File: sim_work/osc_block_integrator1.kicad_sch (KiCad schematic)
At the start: 6 parts, among them U2 LM4562

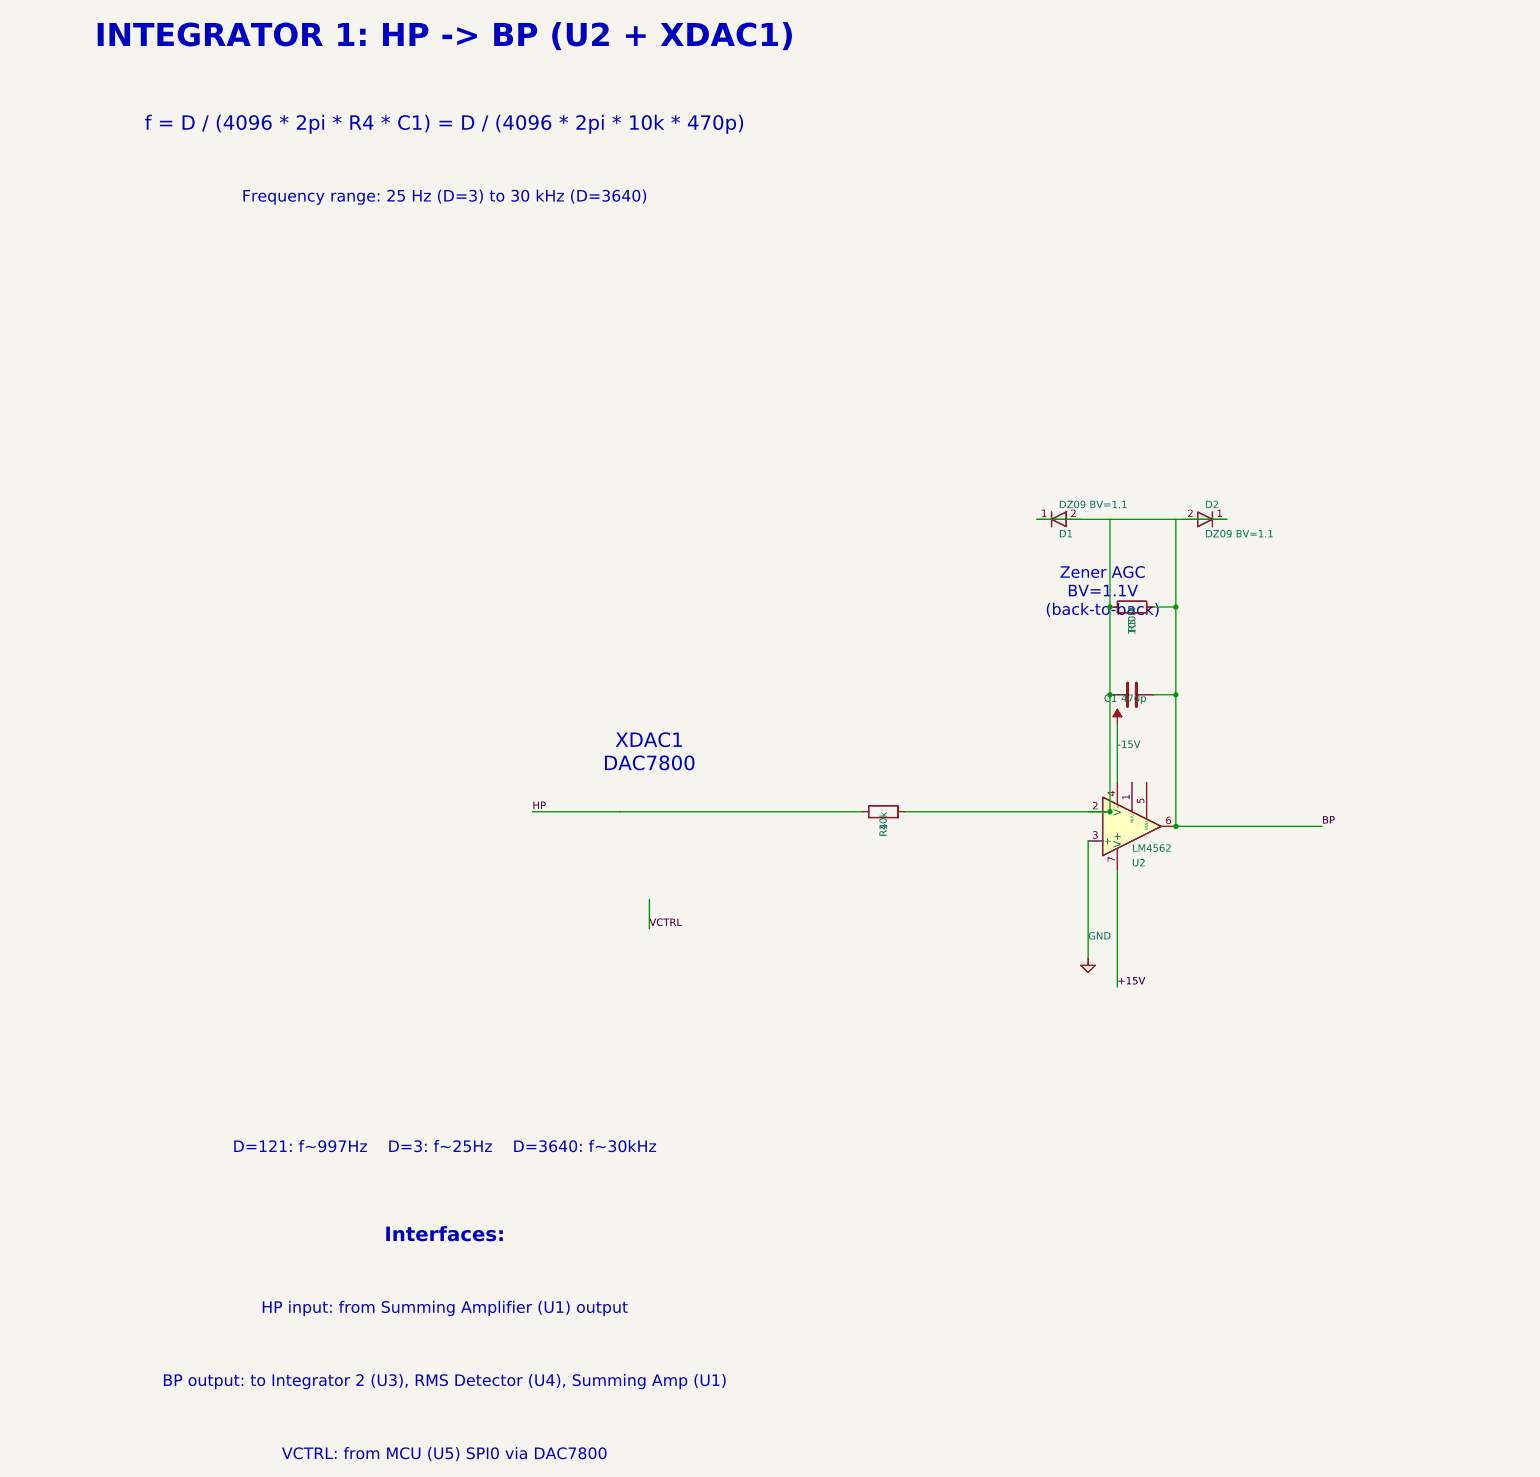
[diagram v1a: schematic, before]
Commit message: Fix schematic connections, add docs and repo portability
- Input filters: R rotation=90 (horizontal), ESD diode rotations fixed,
  junction dots at cathode-signal connection, wires to GND symbols
- Relay ladder: flyback diode rotation 270->90 (K top, A bottom)
- Electrometer/Mux TIA: 4 junction dots each at T-junctions
- AD636 RMS detector: proper IC box with pin labels replaces text-only
- Oscillator blocks: D_Zener symbol, L-shaped cathode routing
- TIA blocks: title/function annotations on all 5 blocks
- New: requirements.txt, docs/oscillator_guide.md
- D_Zener.kicad_sym added to bundled symbols/
- .gitignore updated for docs/ and requirements.txt
- README updated with pip install -r requirements.txt
- PROJECT.md session 9 changelog
- SimGUI builds clean (0 errors)

Co-Authored-By: Claude Opus 4.6 <noreply@anthropic.com>
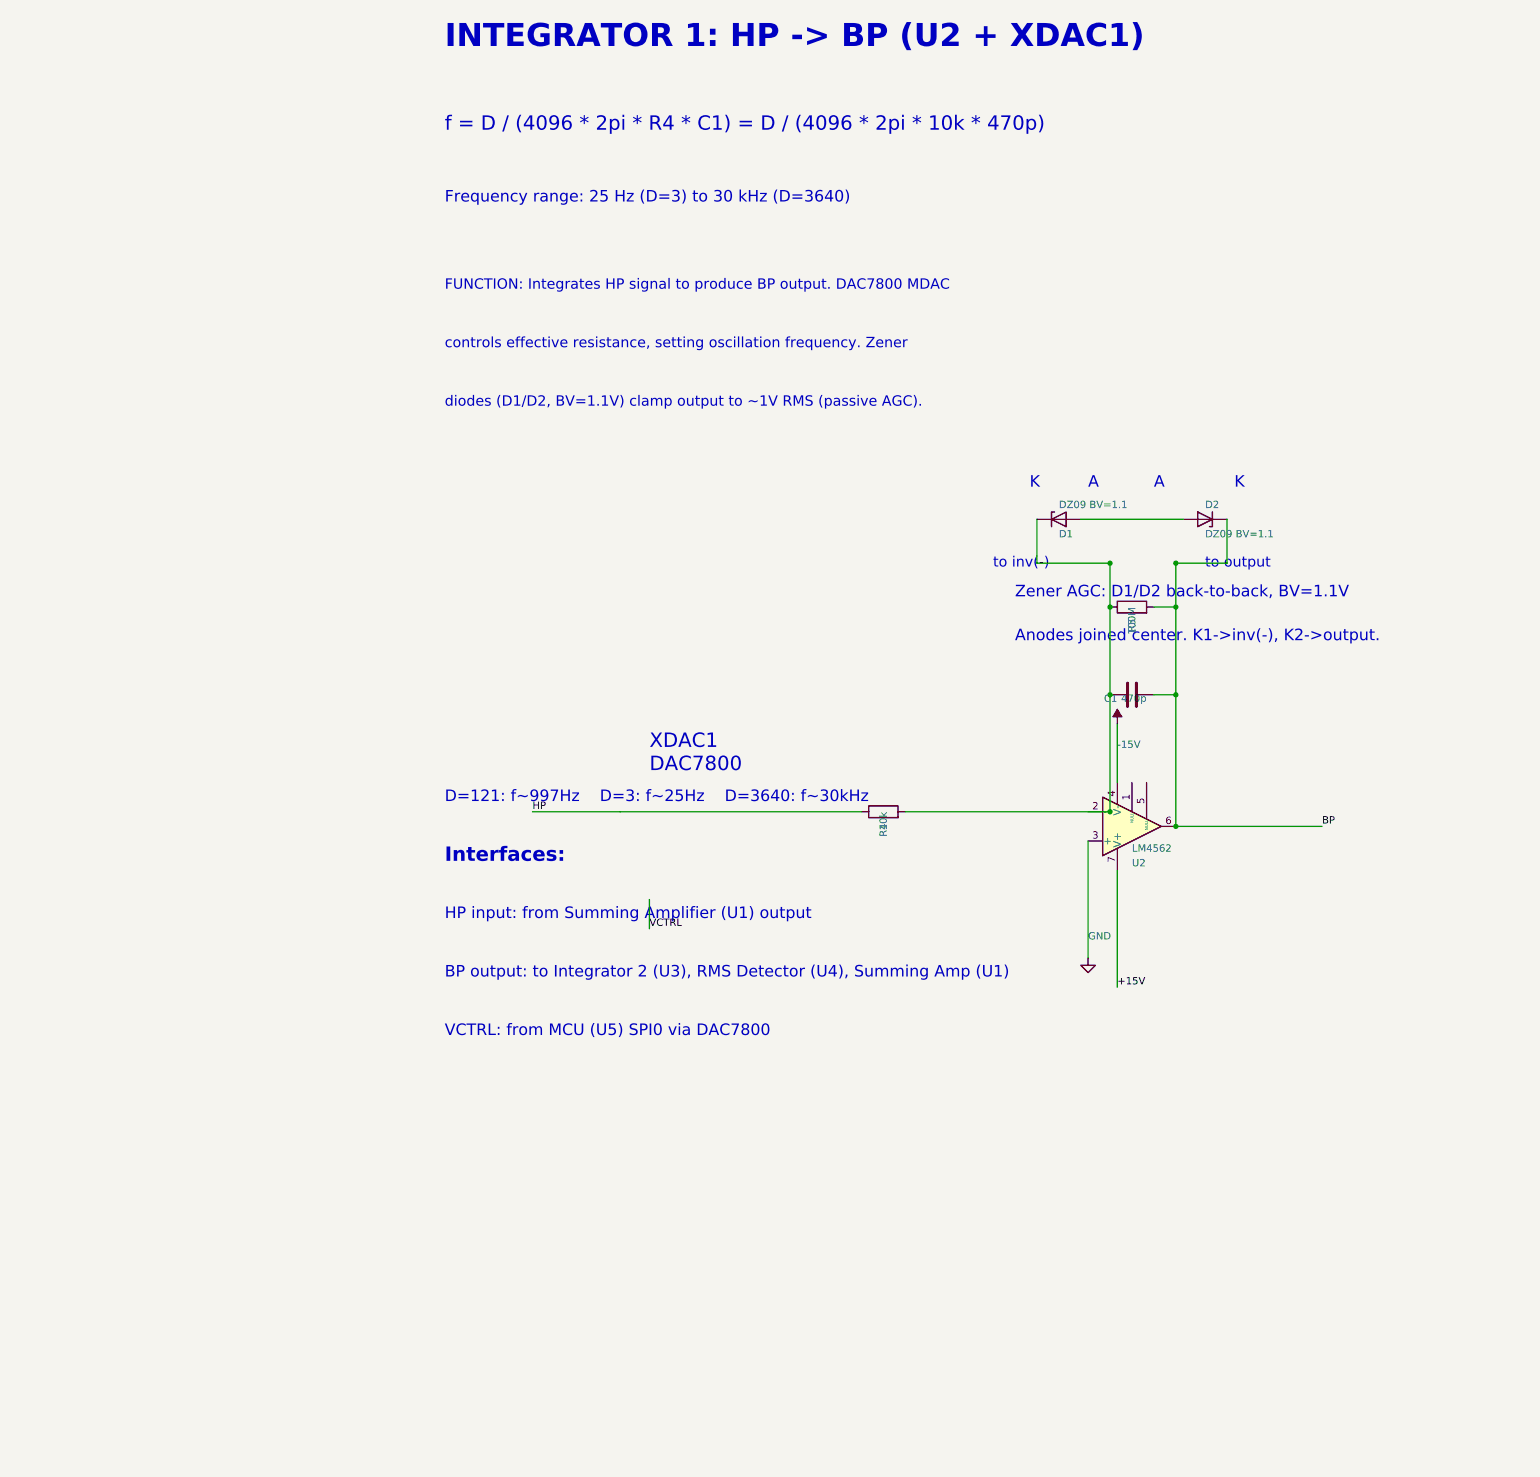
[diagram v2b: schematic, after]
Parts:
- removed D1, D2: DZ09 BV=1.1, symbol D:D
- added D1, D2: DZ09 BV=1.1, symbol D_Zener:D_Zener
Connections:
- net BP: now also D2.1 (K)
- net at C1.1, R4.2, R5.1: now also D1.1 (K)
- new net: D1.2 (A), D2.2 (A)
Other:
- note added: "A"
- note added: "Anodes joined center. K1->inv(-), K2->output."
- note added: "FUNCTION: Integrates HP signal to produce BP output. DAC7800 MDAC"
- note added: "K"
- note added: "Zener AGC: D1/D2 back-to-back, BV=1.1V"
- note added: "controls effective resistance, setting oscillation frequency. Zener"
- note added: "diodes (D1/D2, BV=1.1V) clamp output to ~1V RMS (passive AGC)."
- note added: "to inv(-)"
- note added: "to output"
- note removed: "Zener AGC BV=1.1V (back-to-back)"
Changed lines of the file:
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@@
 		(instances
 			(project "Oscillator - Integrator 1"
-				(path "/9a37c2ac-4e1b-41c6-911d-1272ad46f667"
+				(path "/0aa0564e-5a8b-4527-900e-69c0f4e778f3"
 					(reference "U2")
 					(unit 1)
@@
 		(instances
 			(project "Oscillator - Integrator 1"
-				(path "/9a37c2ac-4e1b-41c6-911d-1272ad46f667"
+				(path "/0aa0564e-5a8b-4527-900e-69c0f4e778f3"
 					(reference "R4")
 					(unit 1)
@@
 		(instances
 			(project "Oscillator - Integrator 1"
-				(path "/9a37c2ac-4e1b-41c6-911d-1272ad46f667"
+				(path "/0aa0564e-5a8b-4527-900e-69c0f4e778f3"
 					(reference "C1")
 					(unit 1)
@@
 		(instances
 			(project "Oscillator - Integrator 1"
-				(path "/9a37c2ac-4e1b-41c6-911d-1272ad46f667"
+				(path "/0aa0564e-5a8b-4527-900e-69c0f4e778f3"
 					(reference "R5")
 					(unit 1)
@@
 	)
 	(symbol
-		(lib_id "D:D")
+		(lib_id "D_Zener:D_Zener")
 		(at 127 99.06 0)
 		(unit 1)
@@
 		(instances
 			(project "Oscillator - Integrator 1"
-				(path "/9a37c2ac-4e1b-41c6-911d-1272ad46f667"
+				(path "/0aa0564e-5a8b-4527-900e-69c0f4e778f3"
 					(reference "D1")
 					(unit 1)
@@
 	)
 	(symbol
-		(lib_id "D:D")
+		(lib_id "D_Zener:D_Zener")
 		(at 152.4 99.06 180)
 		(unit 1)
@@
 		(instances
 			(project "Oscillator - Integrator 1"
-				(path "/9a37c2ac-4e1b-41c6-911d-1272ad46f667"
+				(path "/0aa0564e-5a8b-4527-900e-69c0f4e778f3"
 					(reference "D2")
 					(unit 1)
@@
 		(instances
 			(project "Oscillator - Integrator 1"
-				(path "/9a37c2ac-4e1b-41c6-911d-1272ad46f667"
+				(path "/0aa0564e-5a8b-4527-900e-69c0f4e778f3"
 					(reference "#PWR001")
 					(unit 1)
@@
 		(instances
 			(project "Oscillator - Integrator 1"
-				(path "/9a37c2ac-4e1b-41c6-911d-1272ad46f667"
+				(path "/0aa0564e-5a8b-4527-900e-69c0f4e778f3"
 					(reference "#PWR002")
 					(unit 1)
@@
 	(wire
 		(pts
-			(xy 123.19 99.06) (xy 156.21 99.06)
-		)
-		(stroke
-			(width 0)
-			(type default)
-		)
-	)
-	(wire
-		(pts
-			(xy 135.89 99.06) (xy 135.89 114.3)
-		)
-		(stroke
-			(width 0)
-			(type default)
-		)
-	)
-	(wire
-		(pts
-			(xy 147.32 99.06) (xy 147.32 114.3)
+			(xy 130.81 99.06) (xy 148.59 99.06)
+		)
+		(stroke
+			(width 0)
+			(type default)
+		)
+	)
+	(wire
+		(pts
+			(xy 123.19 99.06) (xy 123.19 106.68)
+		)
+		(stroke
+			(width 0)
+			(type default)
+		)
+	)
+	(wire
+		(pts
+			(xy 123.19 106.68) (xy 135.89 106.68)
+		)
+		(stroke
+			(width 0)
+			(type default)
+		)
+	)
+	(wire
+		(pts
+			(xy 135.89 106.68) (xy 135.89 114.3)
+		)
+		(stroke
+			(width 0)
+			(type default)
+		)
+	)
+	(wire
+		(pts
+			(xy 156.21 99.06) (xy 156.21 106.68)
+		)
+		(stroke
+			(width 0)
+			(type default)
+		)
+	)
+	(wire
+		(pts
+			(xy 147.32 106.68) (xy 156.21 106.68)
+		)
+		(stroke
+			(width 0)
+			(type default)
+		)
+	)
+	(wire
+		(pts
+			(xy 147.32 106.68) (xy 147.32 114.3)
 		)
 		(stroke
@@
 	)
 	(junction
+		(at 135.89 106.68)
+		(diameter 0)
+		(color 0 0 0 0)
+	)
+	(junction
 		(at 135.89 114.3)
+		(diameter 0)
+		(color 0 0 0 0)
+	)
+	(junction
+		(at 147.32 106.68)
 		(diameter 0)
 		(color 0 0 0 0)
@@
 				(bold yes)
 			)
+			(justify left)
 		)
 	)
@@
 				(size 2.5 2.5)
 			)
+			(justify left)
 		)
 	)
@@
 				(size 2 2)
 			)
+			(justify left)
+		)
+	)
+	(text "FUNCTION: Integrates HP signal to produce BP output. DAC7800 MDAC"
+		(exclude_from_sim no)
+		(at 20.32 58.42 0.0000)
+		(effects
+			(font
+				(size 1.8 1.8)
+			)
+			(justify left)
+		)
+	)
+	(text "controls effective resistance, setting oscillation frequency. Zener"
+		(exclude_from_sim no)
+		(at 20.32 68.58 0.0000)
+		(effects
+			(font
+				(size 1.8 1.8)
+			)
+			(justify left)
+		)
+	)
+	(text "diodes (D1/D2, BV=1.1V) clamp output to ~1V RMS (passive AGC)."
+		(exclude_from_sim no)
+		(at 20.32 78.74 0.0000)
+		(effects
+			(font
+				(size 1.8 1.8)
+			)
+			(justify left)
 		)
 	)
@@
 				(size 2.5 2.5)
 			)
-		)
-	)
-	(text "Zener AGC\nBV=1.1V\n(back-to-back)"
-		(exclude_from_sim no)
-		(at 134.62 111.76 0.0000)
-		(effects
-			(font
-				(size 2 2)
-			)
+			(justify left)
+		)
+	)
+	(text "K"
+		(exclude_from_sim no)
+		(at 121.92 92.71 0.0000)
+		(effects
+			(font
+				(size 2 2)
+			)
+			(justify left)
+		)
+	)
+	(text "A"
+		(exclude_from_sim no)
+		(at 132.08 92.71 0.0000)
+		(effects
+			(font
+				(size 2 2)
+			)
+			(justify left)
+		)
+	)
+	(text "A"
+		(exclude_from_sim no)
+		(at 143.51 92.71 0.0000)
+		(effects
+			(font
+				(size 2 2)
+			)
+			(justify left)
+		)
+	)
+	(text "K"
+		(exclude_from_sim no)
+		(at 157.48 92.71 0.0000)
+		(effects
+			(font
+				(size 2 2)
+			)
+			(justify left)
+		)
+	)
+	(text "to inv(-)"
+		(exclude_from_sim no)
+		(at 115.57 106.68 0.0000)
+		(effects
+			(font
+				(size 1.8 1.8)
+			)
+			(justify left)
+		)
+	)
+	(text "to output"
+		(exclude_from_sim no)
+		(at 152.4 106.68 0.0000)
+		(effects
+			(font
+				(size 1.8 1.8)
+			)
+			(justify left)
+		)
+	)
+	(text "Zener AGC: D1/D2 back-to-back, BV=1.1V"
+		(exclude_from_sim no)
+		(at 119.38 111.76 0.0000)
+		(effects
+			(font
+				(size 2 2)
+			)
+			(justify left)
+		)
+	)
+	(text "Anodes joined center. K1->inv(-), K2->output."
+		(exclude_from_sim no)
+		(at 119.38 119.38 0.0000)
+		(effects
+			(font
+				(size 2 2)
+			)
+			(justify left)
 		)
 	)
 	(text "D=121: f~997Hz    D=3: f~25Hz    D=3640: f~30kHz"
 		(exclude_from_sim no)
-		(at 20.32 208.28 0.0000)
-		(effects
-			(font
-				(size 2 2)
-			)
+		(at 20.32 147.32 0.0000)
+		(effects
+			(font
+				(size 2 2)
+			)
+			(justify left)
 		)
 	)
 	(text "Interfaces:"
 		(exclude_from_sim no)
-		(at 20.32 223.52 0.0000)
+		(at 20.32 157.48 0.0000)
 		(effects
 			(font
@@
 				(bold yes)
 			)
+			(justify left)
 		)
 	)
 	(text "HP input: from Summing Amplifier (U1) output"
 		(exclude_from_sim no)
-		(at 20.32 236.22 0.0000)
-		(effects
-			(font
-				(size 2 2)
-			)
+		(at 20.32 167.64 0.0000)
+		(effects
+			(font
+				(size 2 2)
+			)
+			(justify left)
 		)
 	)
 	(text "BP output: to Integrator 2 (U3), RMS Detector (U4), Summing Amp (U1)"
 		(exclude_from_sim no)
-		(at 20.32 248.92 0.0000)
-		(effects
-			(font
-				(size 2 2)
-			)
+		(at 20.32 177.8 0.0000)
+		(effects
+			(font
+				(size 2 2)
+			)
+			(justify left)
 		)
 	)
 	(text "VCTRL: from MCU (U5) SPI0 via DAC7800"
 		(exclude_from_sim no)
-		(at 20.32 261.62 0.0000)
-		(effects
-			(font
-				(size 2 2)
-			)
-		)
-	)
+		(at 20.32 187.96 0.0000)
+		(effects
+			(font
+				(size 2 2)
+			)
+			(justify left)
+		)
+	)
